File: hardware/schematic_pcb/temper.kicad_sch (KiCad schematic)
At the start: 50 parts, among them J1 conn_01x03, J2 conn_01x03, J3 conn_01x03, J4 conn_01x03, J5 Charge Connector, J6 MCU Serial I/F, J7 Conn_01x10, M1 AO3401A, Q1 2N7002, Q2 2N7002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

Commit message: Add pullup resistors on DHT22 data lines as temp readings were not reliable.
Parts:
- added R18, R19, R20, R21: 1k, Resistor_SMD:R_0402_1005Metric_Pad0.72x0.64mm_HandSolder, symbol Device:R
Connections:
- net DHT22_1: now also R18.1
- net DHT22_2: now also R19.1
- net DHT22_3: now also R20.1
- net DHT22_4: now also R21.1
- net at C1.1, C8.1, J1.3 (Pin_3)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: now also R18.2, R19.2, R20.2, R21.2

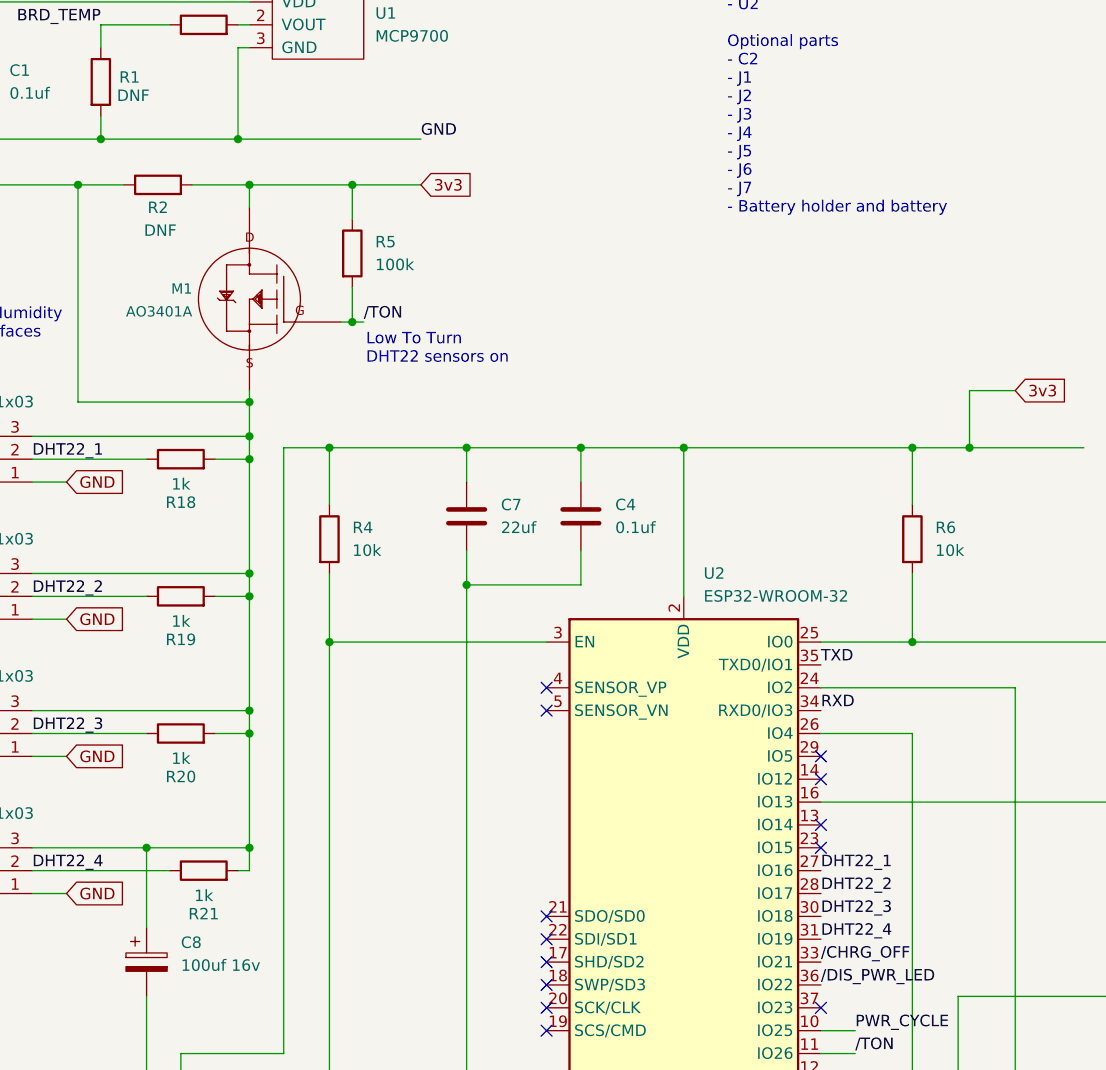
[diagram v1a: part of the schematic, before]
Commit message: Spin PCB: Power sensors from 5v (3.3v pullups) to allow sensors to sit on the end of longer cables without locking up.
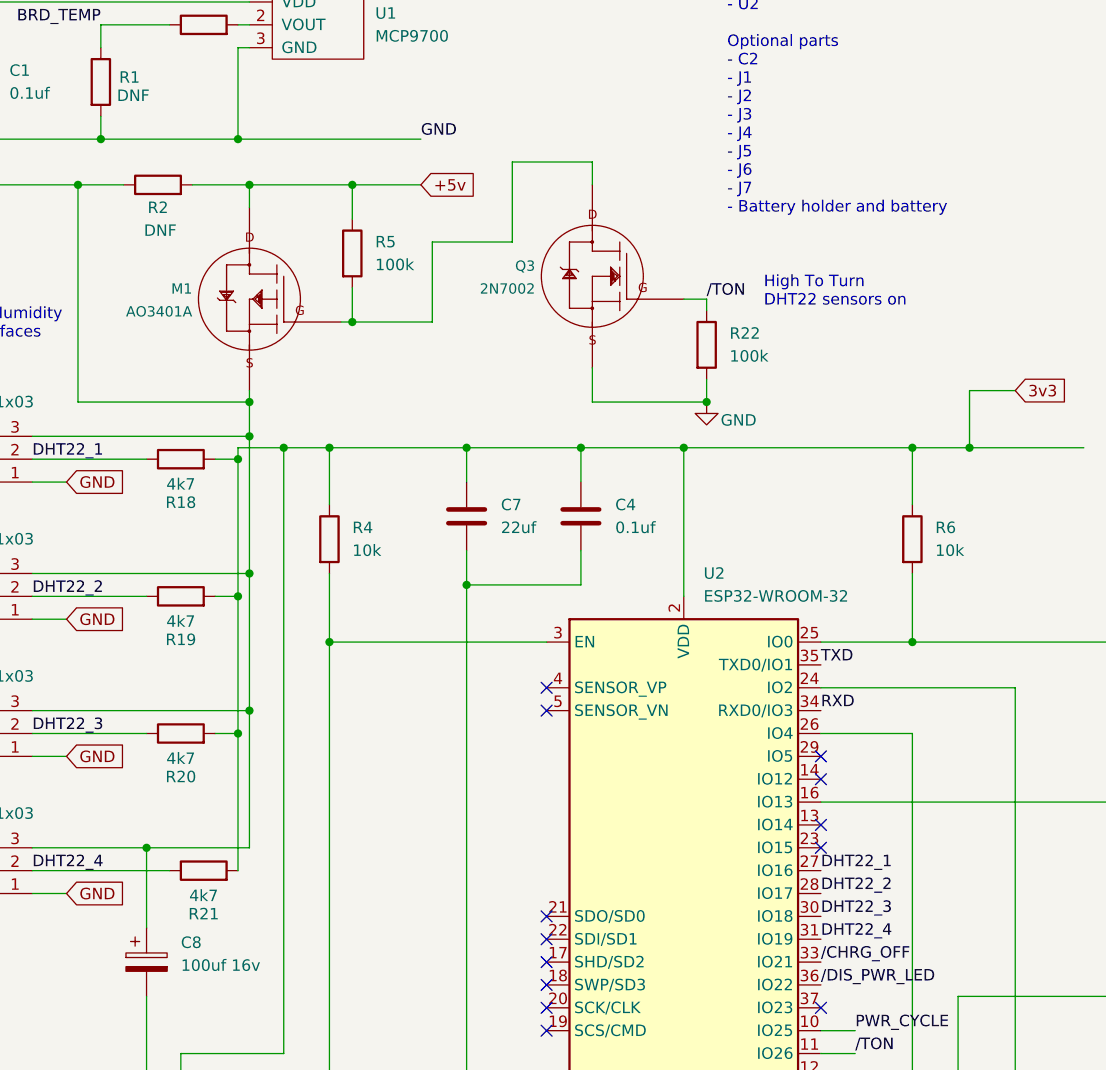
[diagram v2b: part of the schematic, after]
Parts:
- added Q3: 2N7002, Package_TO_SOT_SMD:SOT-23-3, symbol pja_1:2N7002
- added R22: 100k, Resistor_SMD:R_0402_1005Metric_Pad0.72x0.64mm_HandSolder, symbol Device:R
- R18, R19, R20, R21: value 1k -> 4k7; LCSC C25744 -> C25900
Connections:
- net +5v: now also M1.3 (D1), R2.2, R5.1
- net 3v3: now also R18.2, R19.2, R20.2, R21.2; no longer M1.3 (D1), R2.2, R5.1
- net GND: now also Q3.2 (S), R22.2
- net /TON: now also Q3.1 (G), R22.1; no longer M1.1 (G1), R5.2
- net at C1.1, C8.1, J1.3 (Pin_3)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: no longer R18.2, R19.2, R20.2, R21.2
- new net: M1.1 (G1), Q3.3 (D), R5.2
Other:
- note added: "High To Turn DHT22 sensors on"
- note removed: "Low To Turn DHT22 sensors on"
